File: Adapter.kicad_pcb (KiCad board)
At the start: 6 copper layers, 154.4 x 117.4 mm, 300 parts, among them J1 GD820HTX75P6HB, J3 Control_A, J4 Control_C, J5 Control_B, Q1 BC817, Q2 BC817, Q3 BC817, U1 K7805M-1000R3, U11 LMV7219M5X/NOPB, U2 LM1117GS-5.0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

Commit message: VER2.1 init
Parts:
- C11, C14, C17, C20, C22, C24, C26, R2, R3, R4: moved to B.Cu
- C40, C41, C52, C53, C67, C73, D39, D45: moved to F.Cu
- moved D60 22.9 mm to (141.5, 135.1), turned to 180 degrees
- moved D61 21.8 mm to (194.8, 135.1), turned to 180 degrees
- moved D41 21.4 mm to (134.9, 132.3)
- moved D47 21.4 mm to (181.9, 132.3)
- moved R81 18.3 mm to (128.5, 114.0), turned to 90 degrees
- moved R93 18.3 mm to (175.5, 114.0), turned to 90 degrees
- moved R80 17.7 mm to (128.5, 110.0), turned to 90 degrees
- moved R92 17.7 mm to (175.5, 110.0), turned to 90 degrees
- moved D35 12.6 mm to (87.6, 132.3)
- moved C24 8.63 mm to (151.1, 140.2)
- moved C26 8.63 mm to (198.1, 140.2)
- moved D58 7.94 mm to (94.2, 135.1)
- moved R20 6.35 mm to (145.3, 115.3)
- moved R21 6.35 mm to (140.2, 115.3)
- moved R22 6.35 mm to (142.7, 115.3)
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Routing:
- net ~{RST_B}: track 6.52 -> 134.8 mm, vias 3 -> 4
- net ~{RST_C}: track 6.53 -> 131.1 mm, vias 3 -> 4
- net ~{RST}: track 58.2 -> 147.2 mm, vias 0 -> 2
- net C3: track 2.33 -> 36.5 mm, vias 1 -> 0
- net ~{RST_A}: track 100.6 -> 133.7 mm, vias 3 -> 4
- net C5: track 2.45 -> 30.2 mm, vias 1 -> 0
- net Current_B_out: track 104.4 -> 124.4 mm
- net Current_C_out: track 105.7 -> 124.9 mm
- net Net-(D41-A): track 3.35 -> 17.4 mm
- net Net-(D47-A): track 3.35 -> 17.4 mm
- net Net-(D35-A): track 3.61 -> 17.2 mm
- net Net-(D47-K): track 3.81 -> 15.7 mm
- net -15V_H2: track 8.91 -> 20.0 mm, vias 2 -> 3
- net -15V_H3: track 9.01 -> 20.0 mm, vias 2 -> 3
- net +5V_B: track 7.60 -> 14.6 mm
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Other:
- board text added: "Three phase driver board VER2.1"
- board text added: "VER2.1:"
- board text removed: "1. Разобраться с компонентами BOT"
- board text removed: "3-Phase Driver"
- board text removed: "GD820HTX75P6HB"
- board text removed: "REV.1.0.TEST"
- board text removed: "Three phase driver board VER2.0"

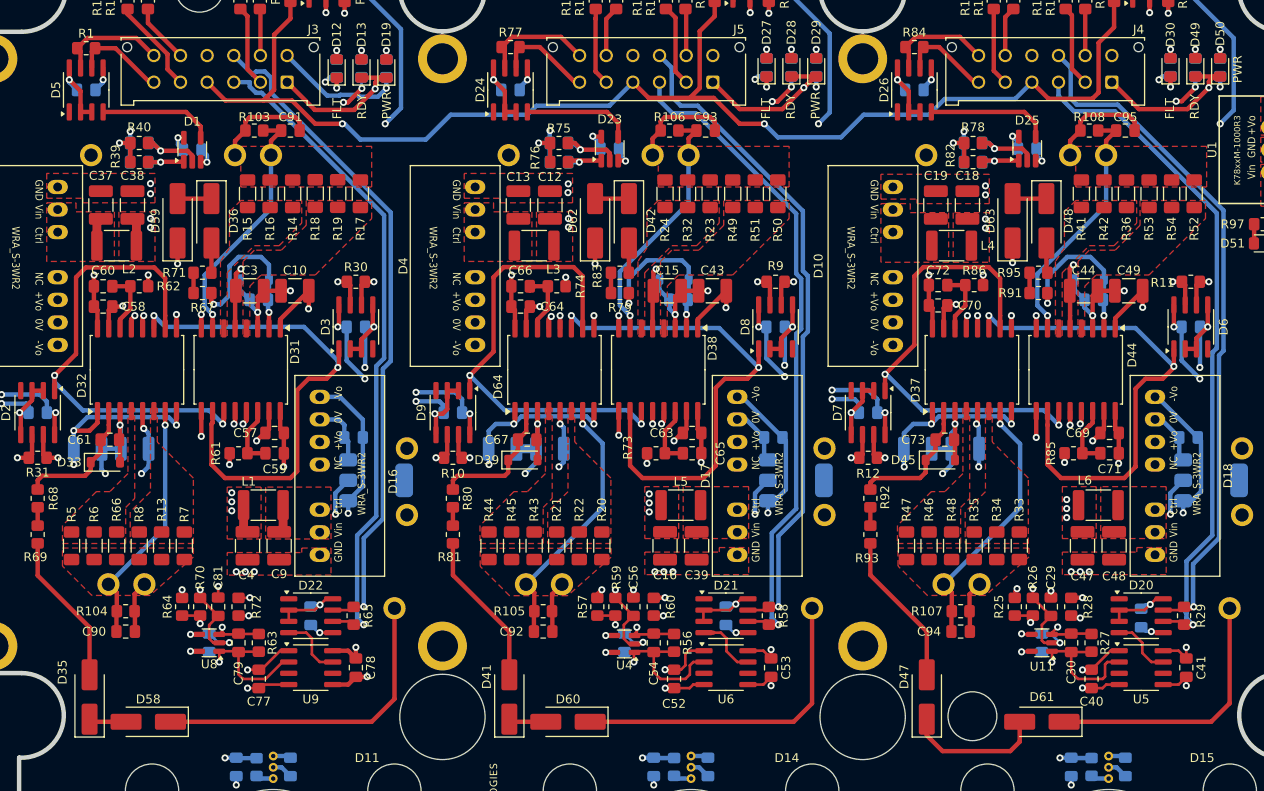
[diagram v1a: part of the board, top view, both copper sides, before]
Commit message: VER2.1: переработал цепь DESAT
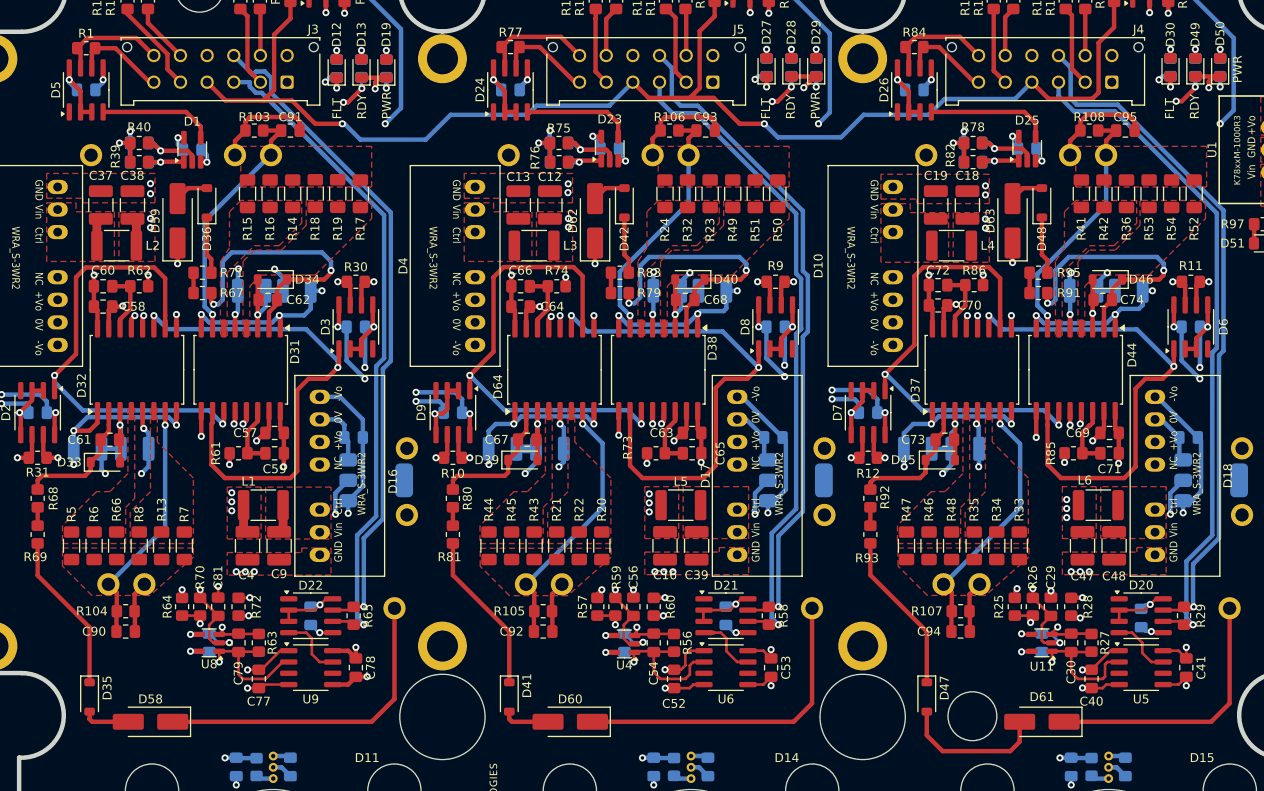
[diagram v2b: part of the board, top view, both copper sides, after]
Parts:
- C10, C15, C3, C43, C44, C49: moved to B.Cu
- C62, C68, C74, D34, D40, D46: moved to F.Cu
- D35, D36, D41, D42, D47, D48: value MURS160 -> MMSZ5232B; footprint Diode_SMD:D_SMA_Handsoldering -> Diode_SMD:D_SOD-123
- R67, R68, R79, R80, R91, R92: value 1.1k -> 2.4k
- moved D36 2.09 mm to (100.8, 76.7), turned to 90 degrees
- moved D42 2.09 mm to (147.8, 76.7), turned to 90 degrees
- moved D48 2.09 mm to (194.8, 76.7), turned to 90 degrees
- moved D46 2.03 mm to (202.2, 85.3)
- moved D34 2.03 mm to (108.2, 85.3)
- moved D40 1.78 mm to (155.2, 85.3)
- moved C62 1.02 mm to (107.7, 87.6)
- moved C74 1.02 mm to (201.7, 87.6)
- moved C68 0.76 mm to (154.7, 87.6)
- moved D58 0.25 mm to (94.5, 135.1)
- moved D60 0.25 mm to (141.7, 135.1)
- moved C10 0.22 mm to (111.0, 86.6)
- moved C3 0.22 mm to (105.9, 86.6)
- turned D35 to -90 degrees
- turned D41 to -90 degrees
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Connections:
- D58 pad 2: Net-(D35-K) -> Net-(D35-A)
- D59 pad 2: Net-(D36-K) -> Net-(D36-A)
- D60 pad 2: Net-(D41-K) -> Net-(D41-A)
- D61 pad 2: Net-(D47-K) -> Net-(D47-A)
- D62 pad 2: Net-(D42-K) -> Net-(D42-A)
- D63 pad 2: Net-(D48-K) -> Net-(D48-A)
- J3 pad 1: GND -> +15V
- J3 pad 7: +15V -> GND
- J4 pad 1: GND -> +15V
- J4 pad 7: +15V -> GND
- J5 pad 1: GND -> +15V
- J5 pad 7: +15V -> GND
- R69 pad 1: Net-(D35-A) -> Net-(D35-K)
- R71 pad 1: Net-(D36-A) -> Net-(D36-K)
- R81 pad 1: Net-(D41-A) -> Net-(D41-K)
- R83 pad 1: Net-(D42-A) -> Net-(D42-K)
- R93 pad 1: Net-(D47-A) -> Net-(D47-K)
- R95 pad 1: Net-(D48-A) -> Net-(D48-K)
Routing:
- net GND: track 244.2 -> 206.7 mm
- net Net-(D41-K): track 4.23 -> 18.3 mm
- net Net-(D35-K): track 4.23 -> 18.1 mm
- net +15V: track 23.6 -> 10.1 mm
- net Net-(D31-DESAT): track 19.4 -> 32.9 mm
- net Net-(D38-DESAT): track 18.8 -> 31.4 mm
- net Net-(D44-DESAT): track 18.6 -> 31.2 mm
- net Net-(D41-A): track 17.4 -> 5.08 mm
- net Net-(D35-A): track 17.2 -> 5.08 mm
- net -15V_L2: track 42.1 -> 52.8 mm, vias 6 -> 7
- net -15V_L1: track 43.0 -> 53.6 mm, vias 6 -> 7
- net -15V_L3: track 41.8 -> 51.9 mm, vias 6 -> 7
- net Net-(D42-K): track 3.81 -> 6.81 mm
- net Net-(D36-K): track 3.81 -> 6.81 mm
- net Net-(D48-K): track 3.81 -> 6.68 mm
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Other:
- board text added: "VER2.1: - Поменял местами +15В и GND в разъёмах; - Вывел на верхнюю сторону всю цепь DESAT; - Разделил все полигоны питания; - Заменил стабилитроны в цепи DESAT;"
- board text removed: "VER2.1:"

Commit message: VER2.1: отправил в резонит
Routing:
- net FLT_B: track 90.1 -> 89.2 mm
